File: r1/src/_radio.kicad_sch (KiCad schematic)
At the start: 49 parts, among them J8 DNP, U9 CC1200, Y2 40Mhz

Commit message: Assign MPN's and LCSC part numbers
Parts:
- C45, C46, C49, C50, C52, C54, C55, C57, C60, C61, C72: Tempco (none) -> C0G
- C47: Tempco (none) -> U2J / UJ / C0G
- C51, C53, C56, C58, C59, C62, C63, C65, C67, C69, C71: Tempco (none) -> X5R
- L10, L3, L6, L8, L9: LCSC (none) -> C82920; MPN (none) -> LQW15AN12NJ00D
- L2: LCSC (none) -> C184029; MPN (none) -> LQW15AN10NJ00D
- L4: LCSC (none) -> C94079; MPN (none) -> LQW15AN15NJ00D
- L5: LCSC (none) -> C82918; MPN (none) -> LQW15AN7N5G00D
- L7: LCSC (none) -> C82917; MPN (none) -> LQW15AN18NJ00D
- U9: LCSC (none) -> C122881; MPN (none) -> CC1200
- Y2: LCSC (none) -> C255943; MPN (none) -> X1E000021017700
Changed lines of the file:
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@@
+      (effects (font (size 1.27 1.27)) hide)
+    )
+    (property "Tempco" "X5R" (at 129.54 53.34 0)
       (effects (font (size 1.27 1.27)) hide)
     )
@@
       (effects (font (size 1.27 1.27)) hide)
     )
+    (property "Tempco" "X5R" (at 139.7 53.34 0)
+      (effects (font (size 1.27 1.27)) hide)
+    )
     (pin "1")
     (pin "2")
@@
       (effects (font (size 1.27 1.27)) hide)
     )
+    (property "Tempco" "X5R" (at 149.86 53.34 0)
+      (effects (font (size 1.27 1.27)) hide)
+    )
     (pin "1")
     (pin "2")
@@
       (effects (font (size 1.27 1.27)) hide)
     )
+    (property "Tempco" "X5R" (at 160.02 53.34 0)
+      (effects (font (size 1.27 1.27)) hide)
+    )
     (pin "1")
     (pin "2")
@@
       (effects (font (size 1.27 1.27)) hide)
     )
+    (property "Tempco" "X5R" (at 170.18 53.34 0)
+      (effects (font (size 1.27 1.27)) hide)
+    )
     (pin "1")
     (pin "2")
@@
       (effects (font (size 1.27 1.27)) hide)
     )
+    (property "Tempco" "X5R" (at 180.34 53.34 0)
+      (effects (font (size 1.27 1.27)) hide)
+    )
     (pin "1")
     (pin "2")
@@
       (effects (font (size 1.27 1.27)) hide)
     )
+    (property "Tempco" "X5R" (at 190.5 53.34 0)
+      (effects (font (size 1.27 1.27)) hide)
+    )
     (pin "1")
     (pin "2")
@@
       (effects (font (size 1.27 1.27)) hide)
     )
+    (property "Tempco" "X5R" (at 200.66 53.34 0)
+      (effects (font (size 1.27 1.27)) hide)
+    )
     (pin "1")
     (pin "2")
@@
       (effects (font (size 1.27 1.27)) hide)
     )
+    (property "Tempco" "X5R" (at 210.82 53.34 0)
+      (effects (font (size 1.27 1.27)) hide)
+    )
     (pin "1")
     (pin "2")
@@
       (effects (font (size 1.27 1.27)) hide)
     )
+    (property "Tempco" "X5R" (at 160.02 88.9 0)
+      (effects (font (size 1.27 1.27)) hide)
+    )
     (pin "1")
     (pin "2")
@@
       (effects (font (size 1.27 1.27)) hide)
     )
+    (property "Tempco" "X5R" (at 170.18 88.9 0)
+      (effects (font (size 1.27 1.27)) hide)
+    )
     (pin "1")
     (pin "2")
@@
       (effects (font (size 1.27 1.27)) hide)
     )
+    (property "MPN" "LQW15AN12NJ00D" (at 160.02 104.14 0)
+      (effects (font (size 1.27 1.27)) hide)
+    )
+    (property "LCSC" "C82920" (at 160.02 104.14 0)
+      (effects (font (size 1.27 1.27)) hide)
+    )
     (pin "1")
     (pin "2")
@@
       (effects (font (size 1.27 1.27)) hide)
     )
+    (property "MPN" "LQW15AN15NJ00D" (at 146.05 97.79 90)
+      (effects (font (size 1.27 1.27)) hide)
+    )
+    (property "LCSC" "C94079 " (at 146.05 97.79 90)
+      (effects (font (size 1.27 1.27)) hide)
+    )
     (pin "1")
     (pin "2")
@@
       (effects (font (size 1.27 1.27)) hide)
     )
+    (property "Tempco" "C0G" (at 151.13 104.14 0)
+      (effects (font (size 1.27 1.27)) hide)
+    )
     (pin "1")
     (pin "2")
@@
       (effects (font (size 1.27 1.27)) hide)
     )
+    (property "MPN" "LQW15AN12NJ00D" (at 140.97 104.14 0)
+      (effects (font (size 1.27 1.27)) hide)
+    )
+    (property "LCSC" "C82920" (at 140.97 104.14 0)
+      (effects (font (size 1.27 1.27)) hide)
+    )
     (pin "1")
     (pin "2")
@@
       (effects (font (size 1.27 1.27)) hide)
     )
+    (property "Tempco" "C0G" (at 132.08 104.14 0)
+      (effects (font (size 1.27 1.27)) hide)
+    )
     (pin "1")
     (pin "2")
@@
       (effects (font (size 1.27 1.27)) hide)
     )
+    (property "Tempco" " U2J / UJ / C0G" (at 63.5 93.98 0)
+      (effects (font (size 1.27 1.27)) hide)
+    )
     (pin "1")
     (pin "2")
@@
     )
     (property "Datasheet" "http://www.ti.com/lit/ds/symlink/cc1200.pdf" (at 80.01 44.45 0)
+      (effects (font (size 1.27 1.27)) hide)
+    )
+    (property "MPN" "CC1200" (at 92.71 73.66 0)
+      (effects (font (size 1.27 1.27)) hide)
+    )
+    (property "LCSC" "C122881" (at 92.71 73.66 0)
       (effects (font (size 1.27 1.27)) hide)
     )
@@
       (effects (font (size 1.27 1.27)) hide)
     )
+    (property "MPN" "X1E000021017700" (at 53.34 73.66 90)
+      (effects (font (size 1.27 1.27)) hide)
+    )
+    (property "LCSC" "C255943" (at 53.34 73.66 90)
+      (effects (font (size 1.27 1.27)) hide)
+    )
     (pin "1")
     (pin "2")
@@
       (effects (font (size 1.27 1.27)) hide)
     )
+    (property "Tempco" "C0G" (at 38.1 68.58 0)
+      (effects (font (size 1.27 1.27)) hide)
+    )
     (pin "1")
     (pin "2")
@@
       (effects (font (size 1.27 1.27)) hide)
     )
+    (property "Tempco" "C0G" (at 38.1 78.74 0)
+      (effects (font (size 1.27 1.27)) hide)
+    )
     (pin "1")
     (pin "2")
@@
       (effects (font (size 1.27 1.27)) hide)
     )
+    (property "Tempco" "C0G" (at 81.28 116.84 0)
+      (effects (font (size 1.27 1.27)) hide)
+    )
     (pin "1")
     (pin "2")
@@
       (effects (font (size 1.27 1.27)) hide)
     )
+    (property "Tempco" "C0G" (at 91.44 116.84 0)
+      (effects (font (size 1.27 1.27)) hide)
+    )
     (pin "1")
     (pin "2")
@@
       (effects (font (size 1.27 1.27)) hide)
     )
+    (property "MPN" "LQW15AN10NJ00D" (at 110.49 123.19 90)
+      (effects (font (size 1.27 1.27)) hide)
+    )
+    (property "LCSC" "C184029 " (at 110.49 123.19 90)
+      (effects (font (size 1.27 1.27)) hide)
+    )
     (pin "1")
     (pin "2")
@@
       (effects (font (size 1.27 1.27)) hide)
     )
+    (property "Tempco" "C0G" (at 135.89 133.35 90)
+      (effects (font (size 1.27 1.27)) hide)
+    )
     (pin "1")
     (pin "2")
@@
       (effects (font (size 1.27 1.27)) hide)
     )
+    (property "LCSC" "C82918" (at 146.05 133.35 90)
+      (effects (font (size 1.27 1.27)) hide)
+    )
+    (property "MPN" "LQW15AN7N5G00D" (at 146.05 133.35 90)
+      (effects (font (size 1.27 1.27)) hide)
+    )
     (pin "1")
     (pin "2")
@@
       (effects (font (size 1.27 1.27)) hide)
     )
+    (property "MPN" "LQW15AN18NJ00D" (at 156.21 133.35 90)
+      (effects (font (size 1.27 1.27)) hide)
+    )
+    (property "LCSC" "C82917" (at 156.21 133.35 90)
+      (effects (font (size 1.27 1.27)) hide)
+    )
     (pin "1")
     (pin "2")
@@
       (effects (font (size 1.27 1.27)) hide)
     )
+    (property "Tempco" "C0G" (at 146.05 142.24 90)
+      (effects (font (size 1.27 1.27)) hide)
+    )
     (pin "1")
     (pin "2")
@@
     )
     (property "Datasheet" "~" (at 151.13 124.46 0)
+      (effects (font (size 1.27 1.27)) hide)
+    )
+    (property "Tempco" "C0G" (at 151.13 124.46 0)
       (effects (font (size 1.27 1.27)) hide)
     )
@@
       (effects (font (size 1.27 1.27)) hide)
     )
+    (property "Tempco" "C0G" (at 167.64 140.97 0)
+      (effects (font (size 1.27 1.27)) hide)
+    )
     (pin "1")
     (pin "2")
@@
     )
     (property "Datasheet" "~" (at 177.8 133.35 0)
+      (effects (font (size 1.27 1.27)) hide)
+    )
+    (property "MPN" "LQW15AN12NJ00D" (at 177.8 133.35 90)
+      (effects (font (size 1.27 1.27)) hide)
+    )
+    (property "LCSC" "C82920" (at 177.8 133.35 90)
       (effects (font (size 1.27 1.27)) hide)
     )
@@
       (effects (font (size 1.27 1.27)) hide)
     )
+    (property "LCSC" "C82920" (at 146.05 114.3 0)
+      (effects (font (size 1.27 1.27)) hide)
+    )
+    (property "MPN" "LQW15AN12NJ00D" (at 146.05 114.3 0)
+      (effects (font (size 1.27 1.27)) hide)
+    )
     (pin "1")
     (pin "2")
@@
       (effects (font (size 1.27 1.27)) hide)
     )
+    (property "Tempco" "C0G" (at 210.82 133.35 90)
+      (effects (font (size 1.27 1.27)) hide)
+    )
     (pin "1")
     (pin "2")
@@
       (effects (font (size 1.27 1.27)) hide)
     )
+    (property "MPN" "LQW15AN12NJ00D" (at 218.44 140.97 0)
+      (effects (font (size 1.27 1.27)) hide)
+    )
+    (property "LCSC" "C82920" (at 218.44 140.97 0)
+      (effects (font (size 1.27 1.27)) hide)
+    )

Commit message: Assign manufacturers
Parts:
- L10, L2, L3, L4, L5, L6, L7, L8, L9: Manufacturer (none) -> Murata
- U9: Manufacturer (none) -> Texas Instruments
- Y2: Manufacturer (none) -> Seiko Epson
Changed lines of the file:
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@@
+      (effects (font (size 1.27 1.27)) hide)
+    )
+    (property "Manufacturer" "Murata" (at 160.02 104.14 0)
       (effects (font (size 1.27 1.27)) hide)
     )
@@
       (effects (font (size 1.27 1.27)) hide)
     )
+    (property "Manufacturer" "Murata" (at 146.05 97.79 90)
+      (effects (font (size 1.27 1.27)) hide)
+    )
     (pin "1")
     (pin "2")
@@
       (effects (font (size 1.27 1.27)) hide)
     )
+    (property "Manufacturer" "Murata" (at 140.97 104.14 0)
+      (effects (font (size 1.27 1.27)) hide)
+    )
     (pin "1")
     (pin "2")
@@
     )
     (property "LCSC" "C122881" (at 92.71 73.66 0)
+      (effects (font (size 1.27 1.27)) hide)
+    )
+    (property "Manufacturer" "Texas Instruments" (at 92.71 73.66 0)
       (effects (font (size 1.27 1.27)) hide)
     )
@@
       (effects (font (size 1.27 1.27)) hide)
     )
+    (property "Manufacturer" "Seiko Epson" (at 53.34 73.66 90)
+      (effects (font (size 1.27 1.27)) hide)
+    )
     (pin "1")
     (pin "2")
@@
       (effects (font (size 1.27 1.27)) hide)
     )
+    (property "Manufacturer" "Murata" (at 110.49 123.19 90)
+      (effects (font (size 1.27 1.27)) hide)
+    )
     (pin "1")
     (pin "2")
@@
       (effects (font (size 1.27 1.27)) hide)
     )
+    (property "Manufacturer" "Murata" (at 146.05 133.35 90)
+      (effects (font (size 1.27 1.27)) hide)
+    )
     (pin "1")
     (pin "2")
@@
     )
     (property "LCSC" "C82917" (at 156.21 133.35 90)
+      (effects (font (size 1.27 1.27)) hide)
+    )
+    (property "Manufacturer" "Murata" (at 156.21 133.35 90)
       (effects (font (size 1.27 1.27)) hide)
     )
@@
       (effects (font (size 1.27 1.27)) hide)
     )
+    (property "Manufacturer" "Murata" (at 177.8 133.35 90)
+      (effects (font (size 1.27 1.27)) hide)
+    )
     (pin "1")
     (pin "2")
@@
       (effects (font (size 1.27 1.27)) hide)
     )
+    (property "Manufacturer" "Murata" (at 146.05 114.3 0)
+      (effects (font (size 1.27 1.27)) hide)
+    )
     (pin "1")
     (pin "2")
@@
       (effects (font (size 1.27 1.27)) hide)
     )
+    (property "Manufacturer" "Murata" (at 218.44 140.97 0)
+      (effects (font (size 1.27 1.27)) hide)
+    )

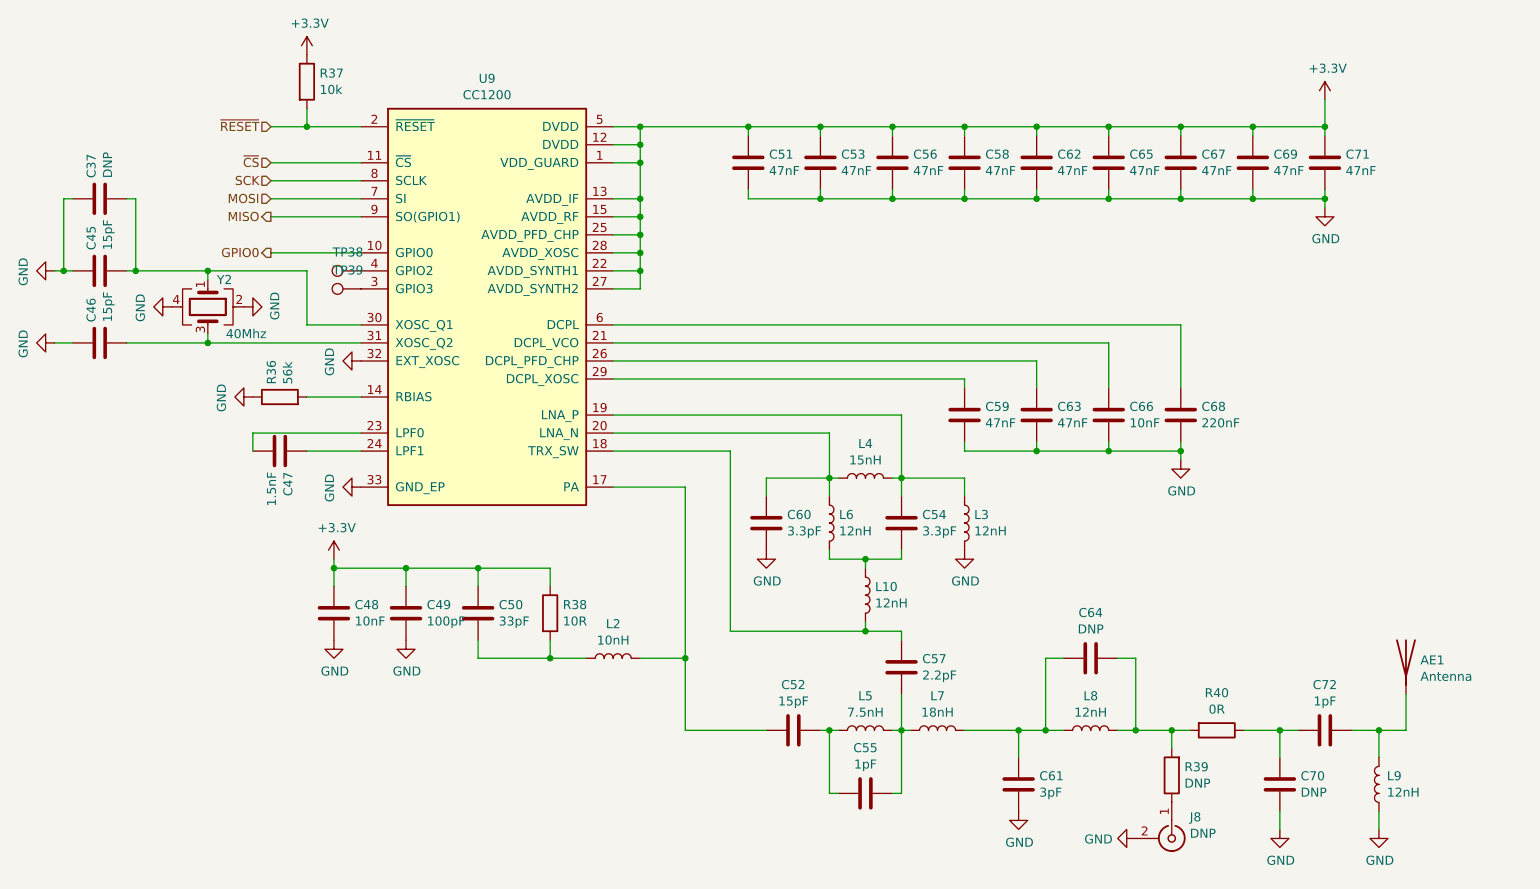
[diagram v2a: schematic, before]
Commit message: Reannotate component refs
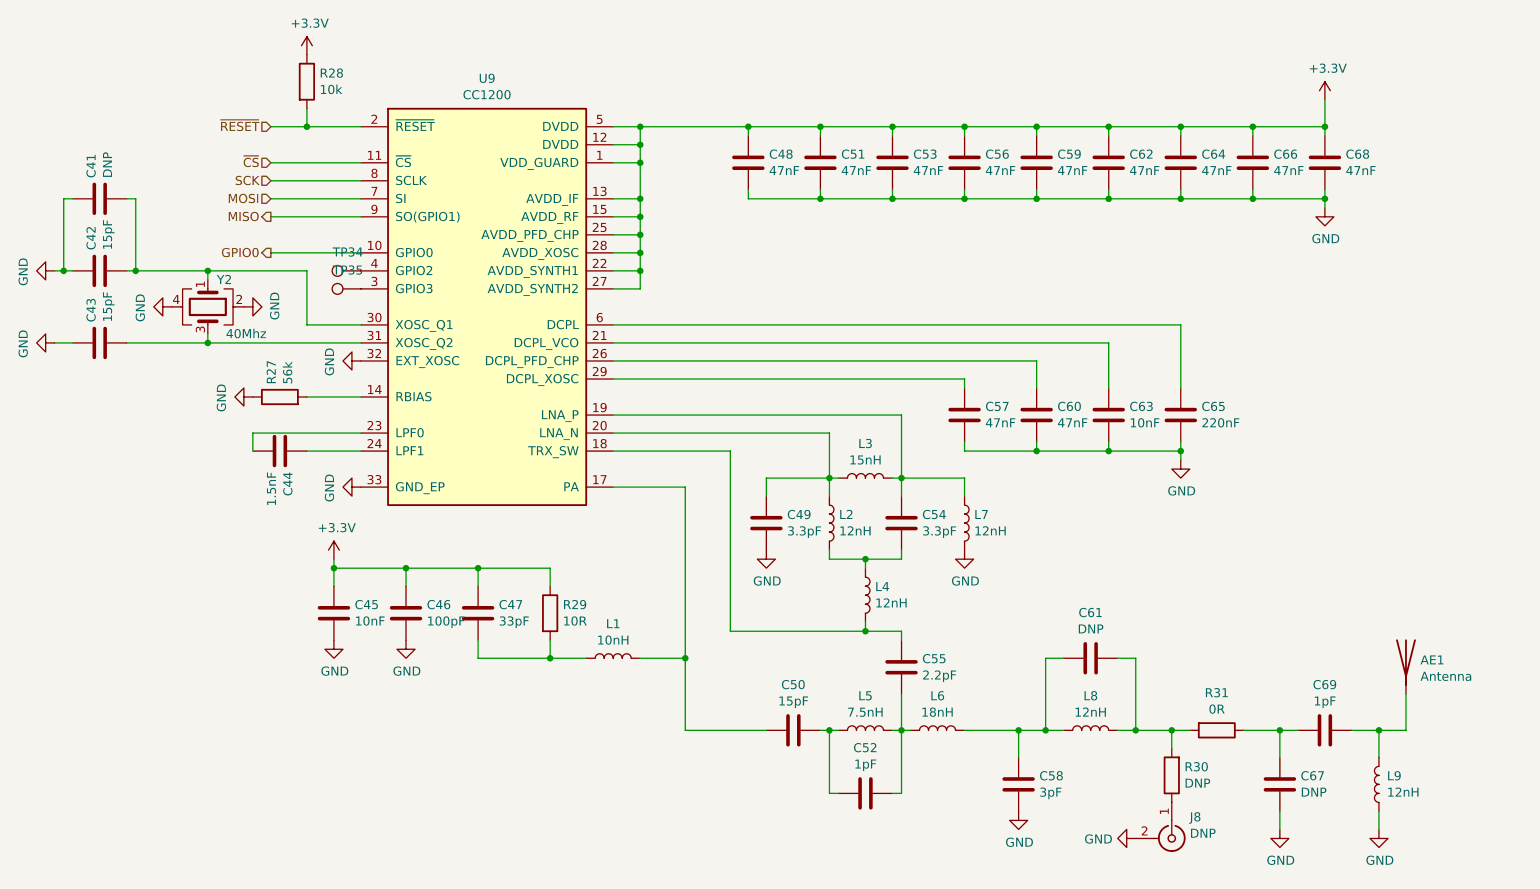
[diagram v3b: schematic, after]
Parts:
- renumbered C37 to C41, C45 to C42, C46 to C43, C47 to C44, C48 to C45, C49 to C46, C50 to C47, C51 to C48, C60 to C49, C52 to C50, C53 to C51, C55 to C52, C56 to C53, C57 to C55, C58 to C56, C59 to C57, C61 to C58, C62 to C59, C63 to C60, C64 to C61, C65 to C62, C66 to C63, C67 to C64, C68 to C65, C69 to C66, C70 to C67, C71 to C68, C72 to C69, L2 to L1, L6 to L2, L4 to L3, L10 to L4, L7 to L6, L3 to L7, R36 to R27, R37 to R28, R38 to R29, R39 to R30, R40 to R31, TP38 to TP34, TP39 to TP35
